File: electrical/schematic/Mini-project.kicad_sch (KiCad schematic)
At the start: 12 parts, among them J1 Connector, SW1 Button 1, SW2 Button 2, U1 L293D Driver, U2 XIAO-ESP32-S3

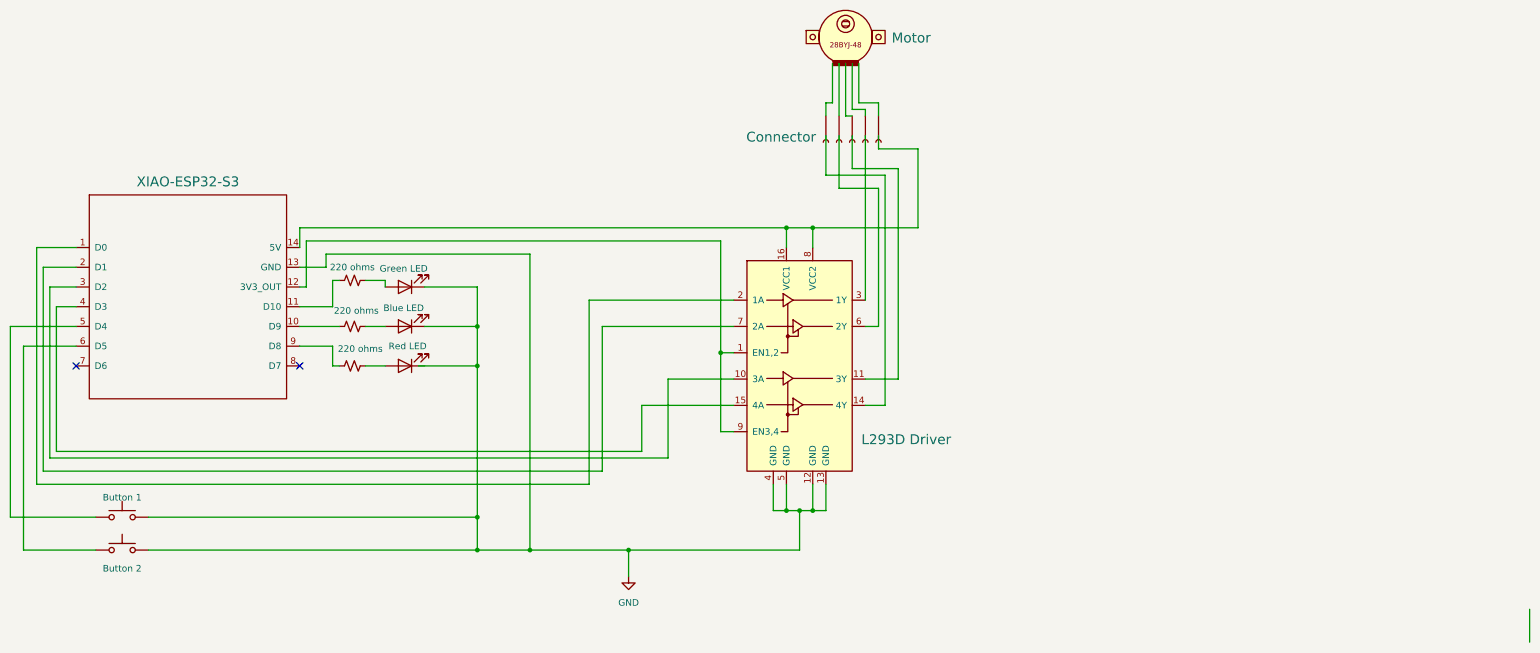
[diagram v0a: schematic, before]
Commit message: electrical schematic version 2 (KiCAD file)
implemented changes documented in schematic_changelog.md
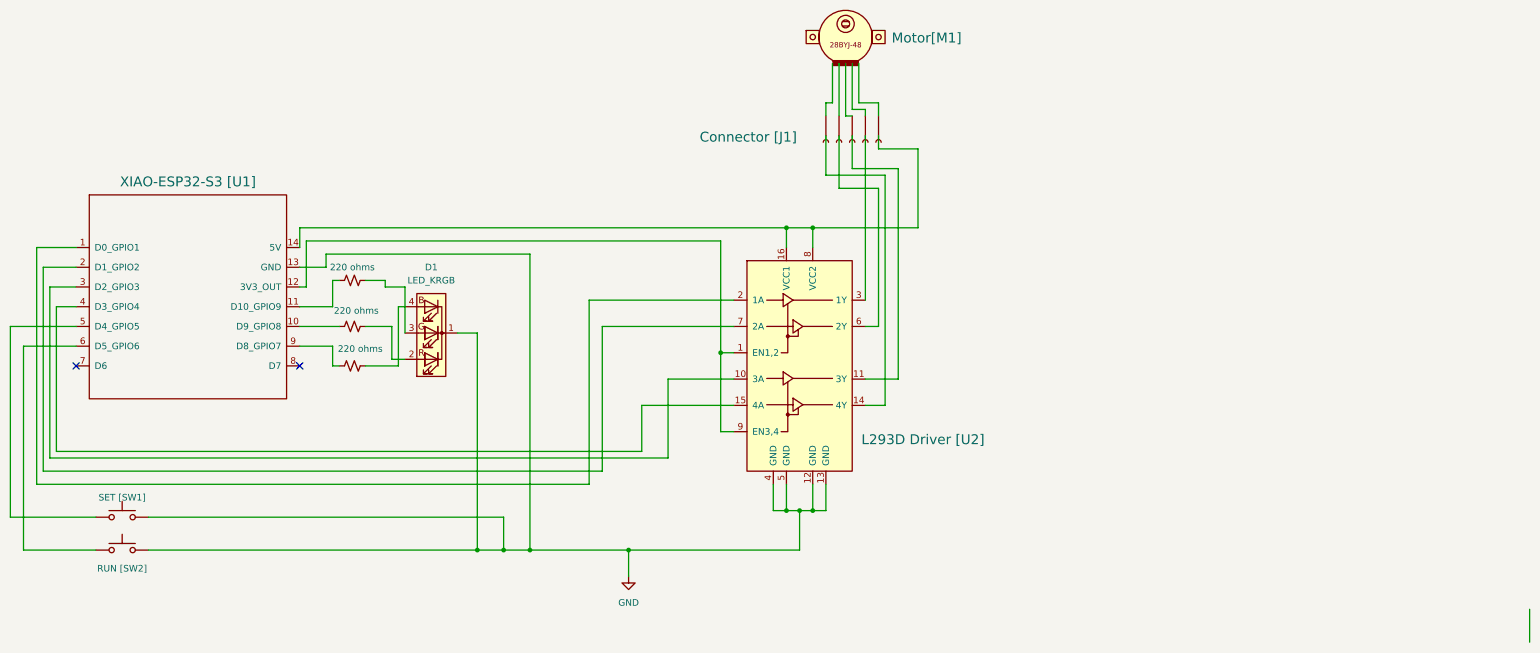
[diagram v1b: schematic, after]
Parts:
- removed D1: Green LED, symbol Device:LED
- removed D2: Red LED, symbol Device:LED
- removed D3: Blue LED, symbol Device:LED
- added D1: LED_KRGB, symbol Device:LED_KRGB
- J1: value Connector -> Connector [J1]
- SW1: value Button 1 -> SET [SW1]
- SW2: value Button 2 -> RUN [SW2]
- U1: value L293D Driver -> L293D Driver [U2]
- U2: value XIAO-ESP32-S3 -> XIAO-ESP32-S3 [U1]
- renumbered Motor to Motor[M1]
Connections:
- net GND: now also D1.1 (K)
- net at R1.2: now also D1.3 (GA)
- net at R3.2: now also D1.4 (BA)
- net at R2.2: now also D1.2 (RA)
